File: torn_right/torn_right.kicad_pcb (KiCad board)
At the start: 2 copper layers, 140.7 x 115.4 mm, 64 parts, among them J2 SJ-43514, J3 Conn_01x04, SW23 SW_Push, SW24 SW_Push, SW25 SW_Push, SW26 SW_Push, SW27 SW_Push, SW28 Rotary_Encoder_Switch, SW29 SW_Push, SW30 SW_Push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

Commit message: preparing for new board revision
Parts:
- J2: footprint footprints:PJ-320A -> footprints:CUI_SJ-43514
- moved J2 7.79 mm to (64.3, 55.9)
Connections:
- U2 pad 11: Net-(U2-Pad11) -> unconnected-(U2-NC-Pad11)
- U2 pad 14: Net-(U2-Pad14) -> unconnected-(U2-NC-Pad14)
- U2 pad 19: Net-(U2-Pad19) -> unconnected-(U2-INTB-Pad19)
- U2 pad 20: Net-(U2-Pad20) -> unconnected-(U2-INTA-Pad20)
- U2 pad 4: Net-(U2-Pad4) -> unconnected-(U2-GPB3-Pad4)
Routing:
- net +5V: track 80.9 -> 92.4 mm
- net /ENC1_B: track 265.1 -> 254.3 mm
- net /COL11: track 231.0 -> 223.1 mm
- net /COL9: track 202.2 -> 196.5 mm
- net /i2c_SCL: track 79.6 -> 74.3 mm
- net /COL6: track 156.9 -> 153.0 mm
- net /i2c_SDA: track 86.6 -> 90.4 mm
- net /COL7: track 166.5 -> 169.7 mm
- net /COL8: track 184.9 -> 187.2 mm
- net /ENC1_A: track 251.3 -> 250.1 mm
- net Net-(D23-A): track 60.2 -> 59.3 mm
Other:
- outline, holes or cut-outs redrawn
- net class Default removed
- net class Power removed
- rule pad_to_mask_clearance: 0.2 -> 0.038
- rule solder_mask_min_width: 0.2 -> 0.1

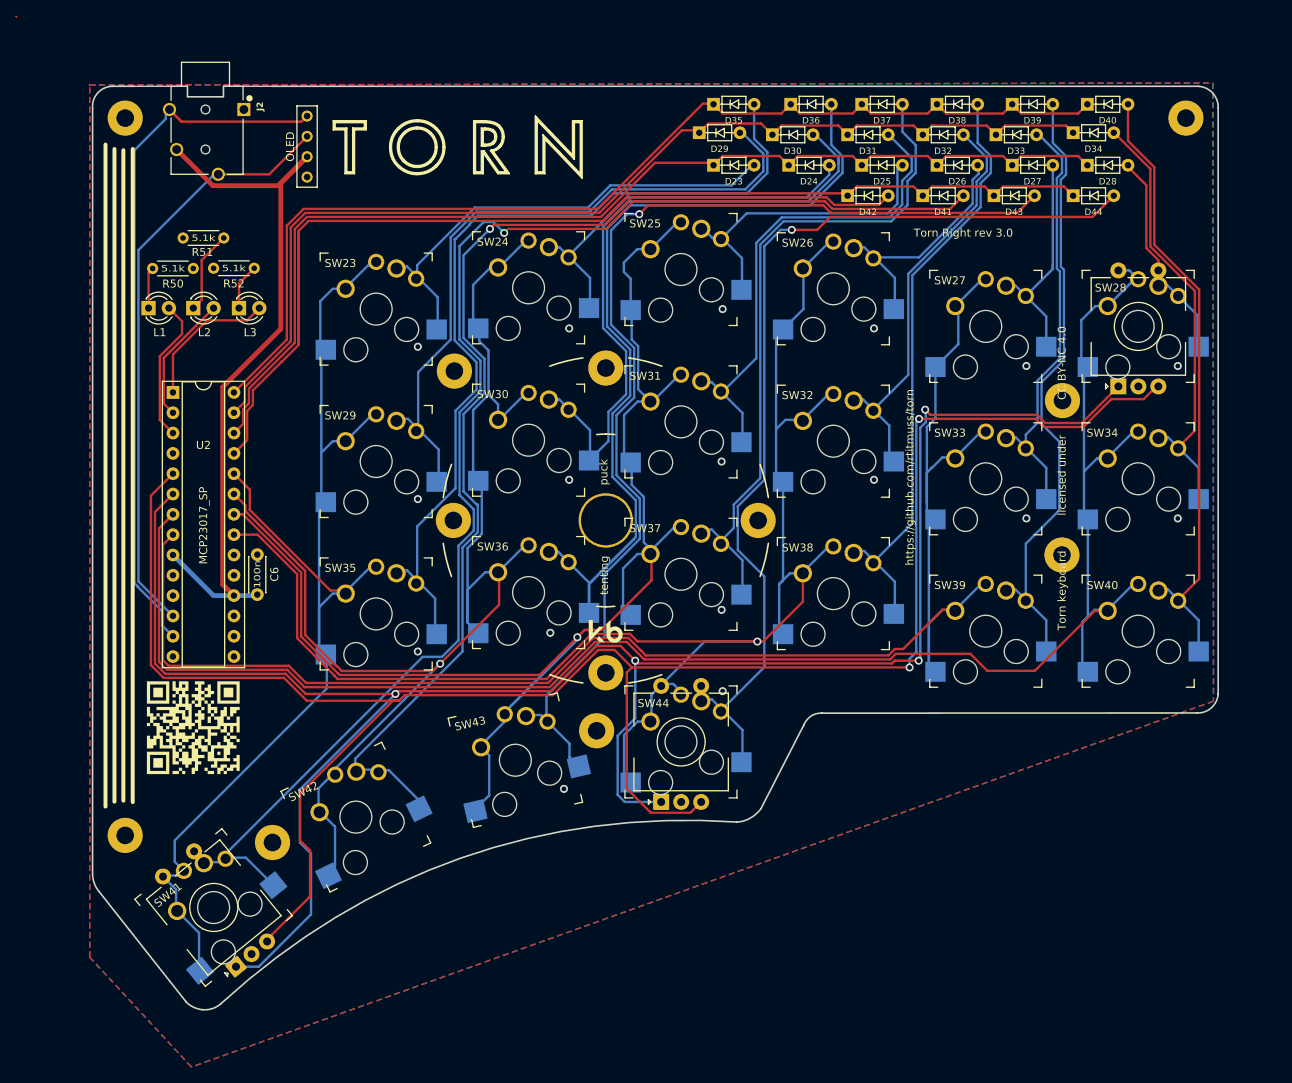
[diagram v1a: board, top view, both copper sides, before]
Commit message: committing before changing to standard size through hole resistors
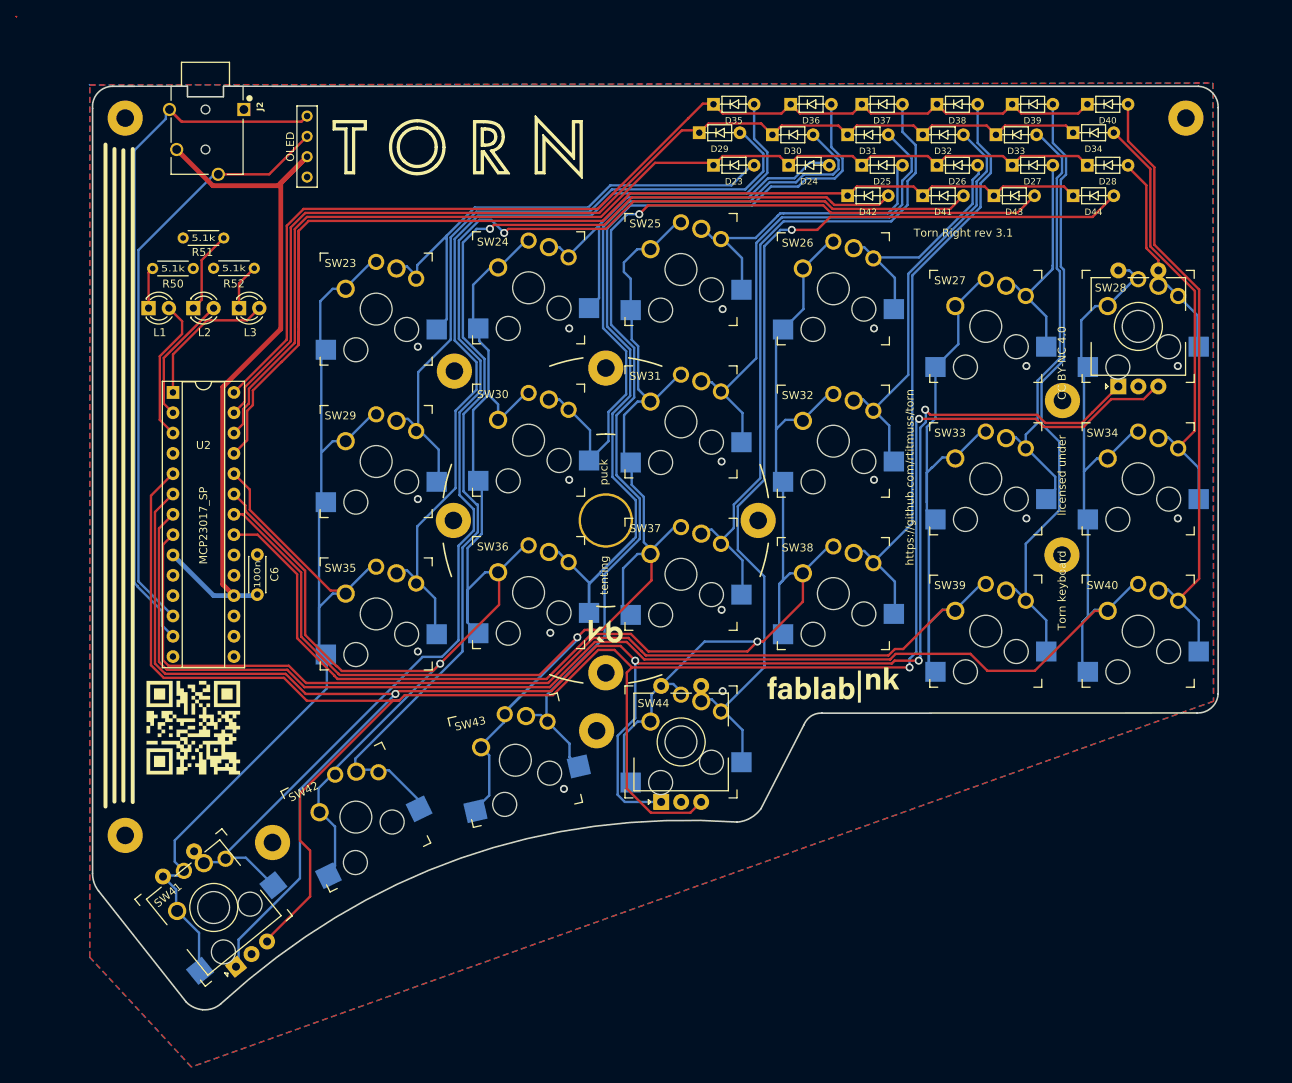
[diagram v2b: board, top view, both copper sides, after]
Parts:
- removed QR1: SYM_Arrow45_Small, footprints:torn_qr_code
- added G***: LOGO, LOGO, F.Cu at (62.7, 130.6)
- added REF**: logo_fablabnk, footprints:logo_fablabnk, F.Cu at (142.1, 126.0)
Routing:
- net Net-(D23-A): track 59.3 -> 64.2 mm
- net Net-(D24-A): track 48.8 -> 51.9 mm
- net /ENC1_A: track 250.1 -> 247.3 mm
- net Net-(D42-A): track 140.9 -> 141.9 mm
- net /COL9: track 196.5 -> 197.5 mm
- net Net-(D30-A): track 83.0 -> 82.0 mm
- net Net-(D33-A): track 53.4 -> 54.3 mm
- net Net-(D41-A): track 173.7 -> 174.5 mm
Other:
- board text added: "Torn Right rev 3.1"
- board text removed: "Torn Right rev 3.0"

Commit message: changed resistor sizes to more common 1/4W 0207DIN sizes on both boards
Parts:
- R50, R51, R52: footprint footprints:R_Axial_DIN0204_L3.6mm_D1.6mm_P5.08mm_Horizontal -> Resistor_THT:R_Axial_DIN0207_L6.3mm_D2.5mm_P7.62mm_Horizontal
- moved R52 8.73 mm to (68.8, 65.2), turned to -90 degrees
- moved R50 8.70 mm to (59.3, 65.2), turned to -90 degrees
- moved R51 4.90 mm to (64.0, 65.2), turned to -90 degrees
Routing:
- net Net-(L2-K): track 10.3 -> 5.86 mm
- net Net-(L1-K): track 5.16 -> 6.23 mm
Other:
- board text added: "Torn Right 42 edition rev 3.1"
- board text added: "Torn keyboard 42 edition licensed under CC BY-NC 4.0"
- board text added: "Torn keyboard licensed under CC BY-NC 4.0 42 edition"
- board text added: "https://github.com/fablabnk/torn"
- board text removed: "Torn Right rev 3.1"
- board text removed: "Torn keyboard licensed under CC BY-NC 4.0"
- board text removed: "https://github.com/rtitmuss/torn"

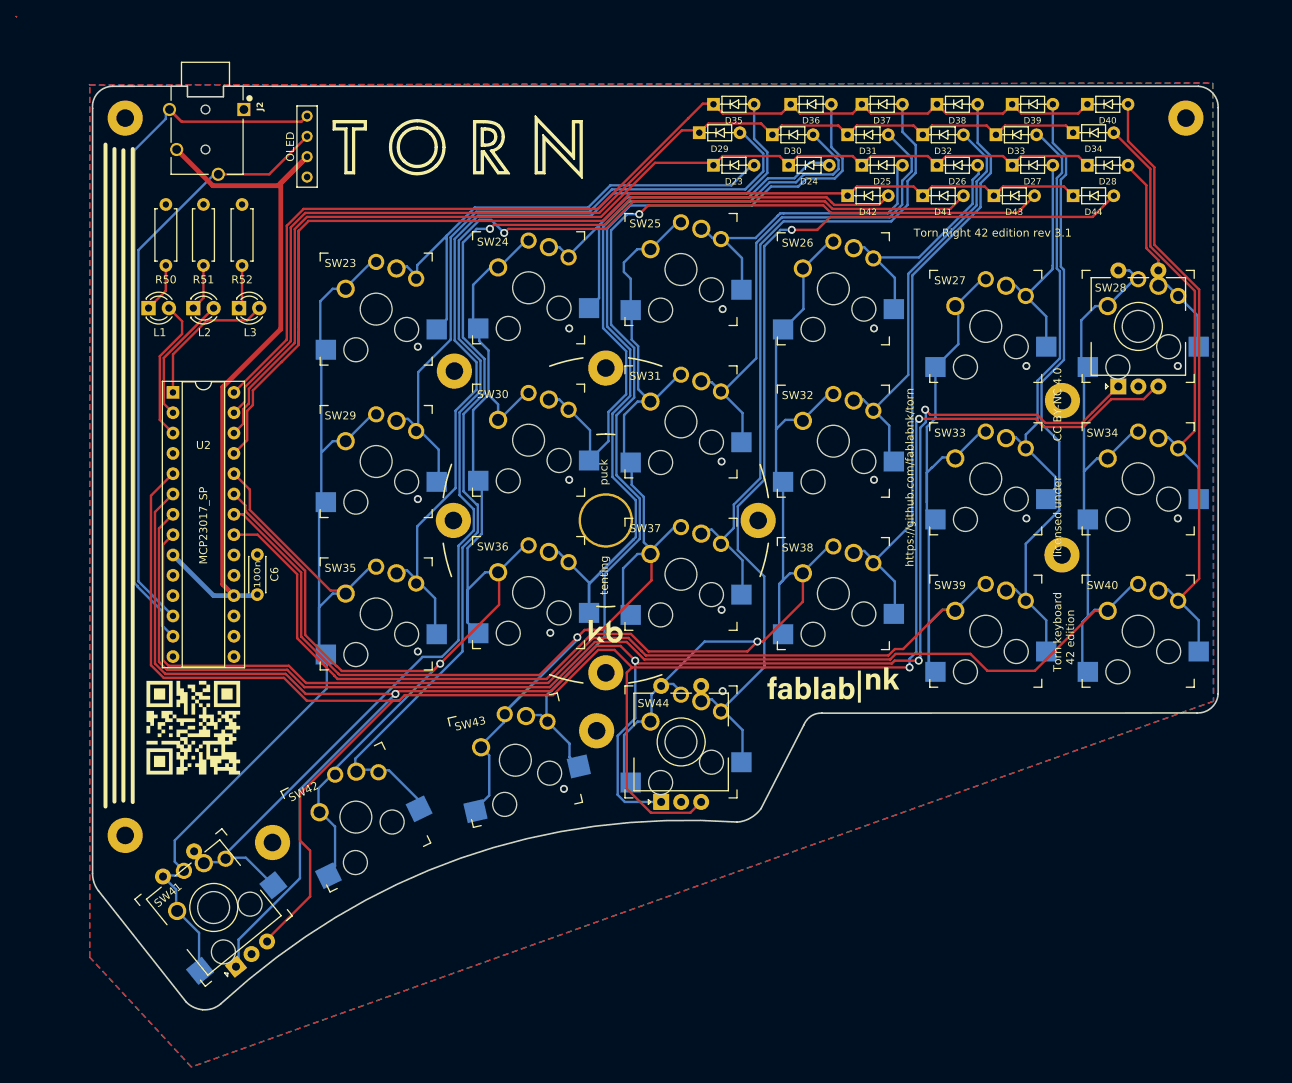
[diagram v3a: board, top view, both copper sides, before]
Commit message: right board updated with proper TRRS and other fixes - reminder to check left side passes DRC
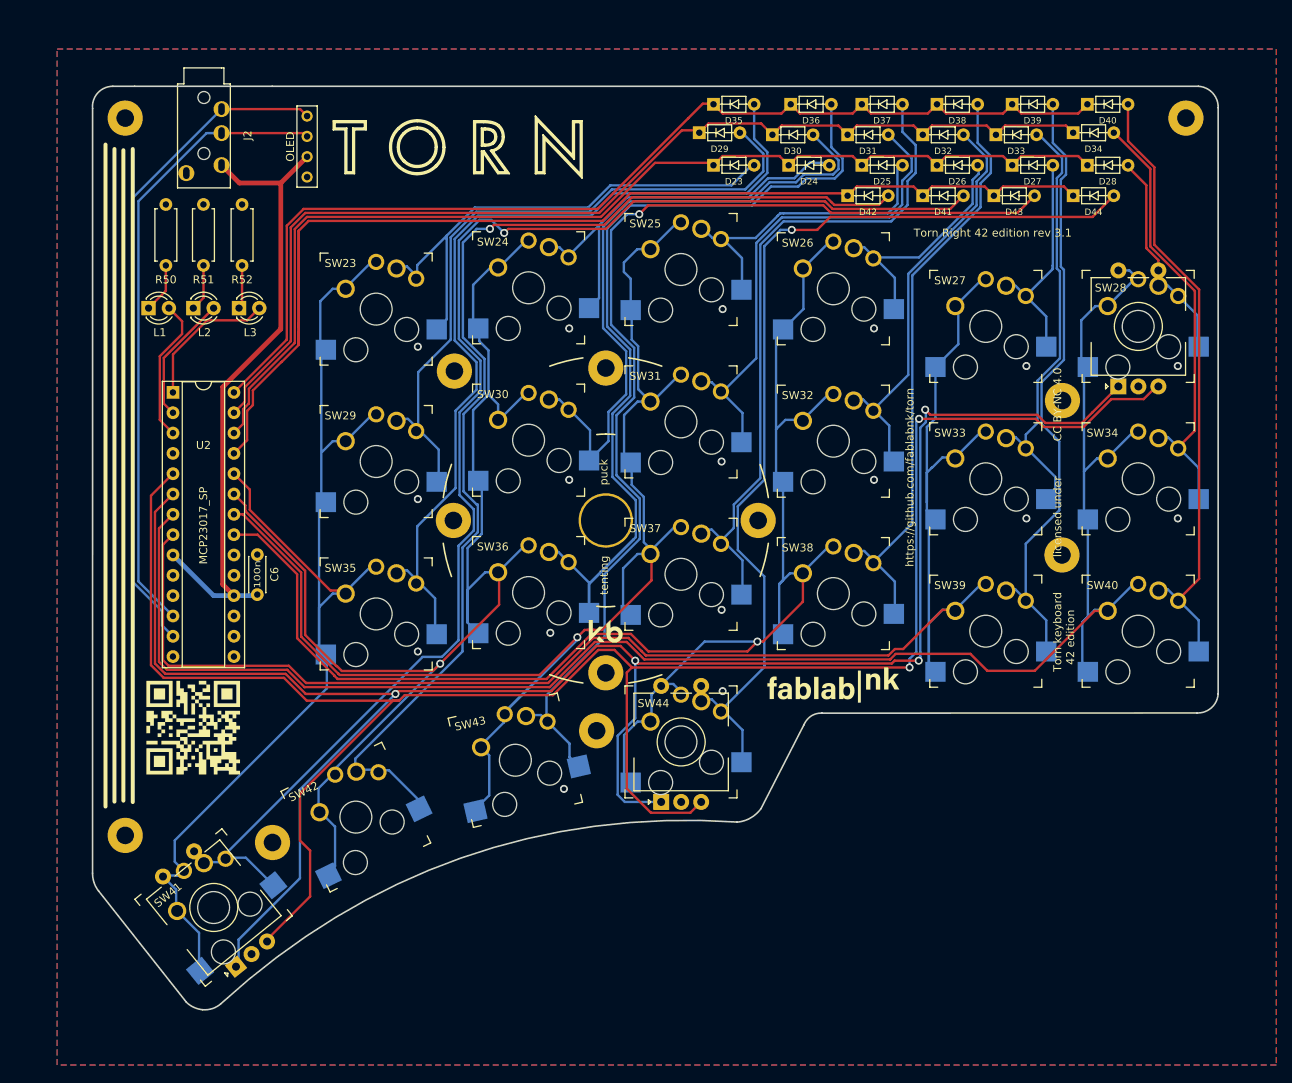
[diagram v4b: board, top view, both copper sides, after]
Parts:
- removed G***: LOGO, LOGO
- added QR1: SYM_Arrow45_Small, footprints:torn_qr_code, F.Cu at (62.7, 130.6)
- J2: footprint footprints:CUI_SJ-43514 -> footprints:PJ-320A
- moved J2 8.05 mm to (66.3, 48.1)
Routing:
- net +5V: track 92.4 -> 81.0 mm
- net /i2c_SDA: track 90.4 -> 83.7 mm
- net /i2c_SCL: track 74.3 -> 78.4 mm
